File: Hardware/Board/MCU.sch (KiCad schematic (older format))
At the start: 1 part

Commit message: Controller auf 100 Pin Version geändert, Pins ersten Funktionen zugeordnet.
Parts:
- removed U?: STM32L475RGTx, Package_QFP:LQFP-64_10x10mm_P0.5mm, symbol MCU_ST_STM32L4:STM32L475RGTx
- added C? (x2): 100nF, symbol Device:C
- added C? (x4): C, symbol Device:C
- added C?: 10nF, symbol Device:C
- added C?: 1uF, symbol Device:C
- added C?: 10uF, symbol Device:C
- added C? (x2): 5p1, symbol Device:C
- added C? (x2): 8p2, symbol Device:C
- added U?: AT25SF081-XMHD-X, Package_SO:TSSOP-8_4.4x3mm_P0.65mm, symbol Memory_Flash:AT25SF081-XMHD-X
- added U?: STM32L475VGTx, Package_QFP:LQFP-100_14x14mm_P0.5mm, symbol MCU_ST_STM32L4:STM32L475VGTx
- added Y?: 32.768, symbol Device:Crystal
- added Y?: 8MHz, symbol Device:Crystal
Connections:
- net labels added: +3.3V, GND, JTAG_RES, JTAG_TCK, JTAG_TDI, JTAG_TDO, JTAG_TMS, QuadSPI_CLK, QuadSPI_IO0, QuadSPI_IO1, QuadSPI_IO2, QuadSPI_IO3, QuadSPI_NCS, RxD-LIN1, RxD-LIN2, RxD-LIN3, RxD-RS485, SCL-1WIRE, SDA-1WIRE, TxD-LIN1, TxD-LIN2, TxD-LIN3, TxD-RS485, USB_D+, USB_D-, USB_ID, USB_NOE, USB_SOF
- wire segments 2 -> 94

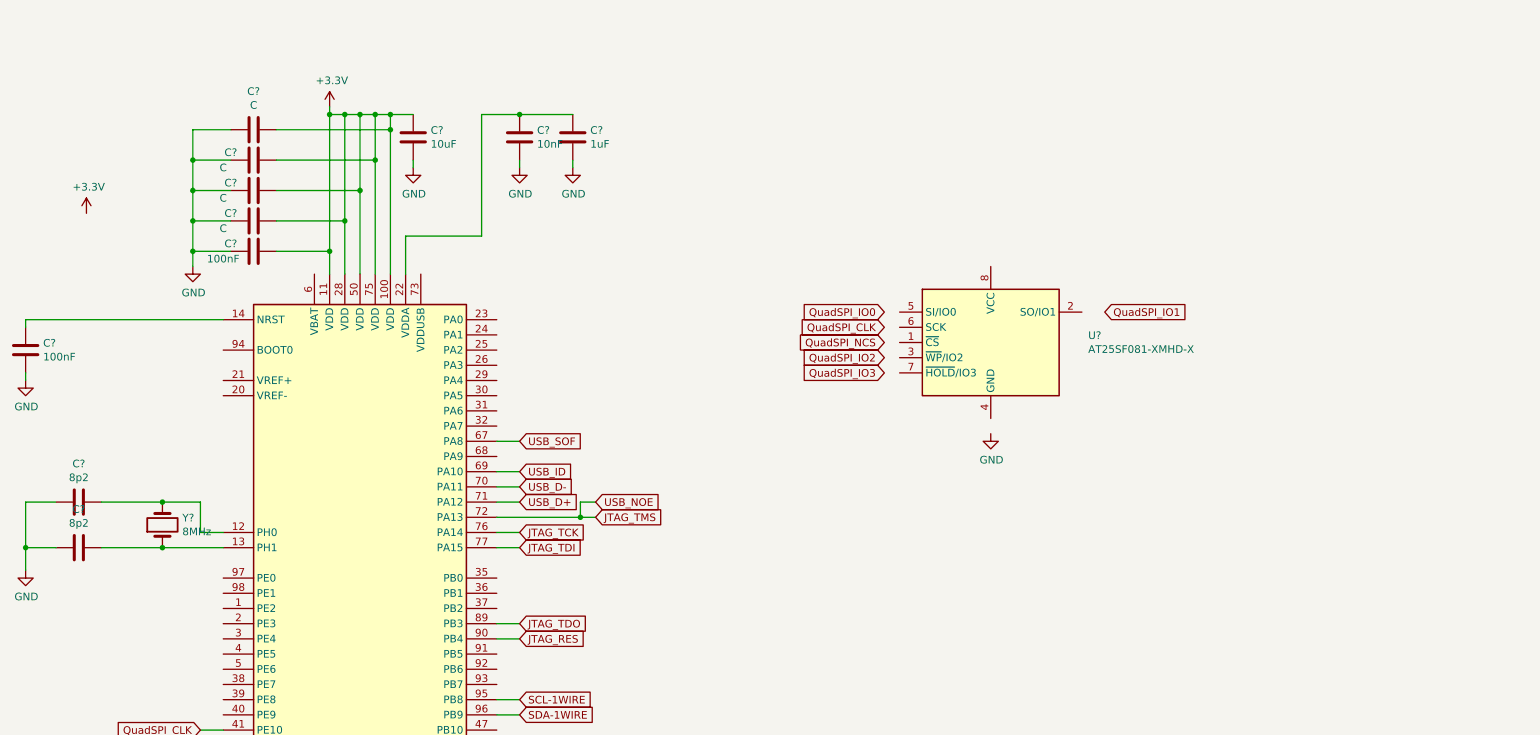
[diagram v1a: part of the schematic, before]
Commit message: JTAG und USB Anschlüsse zugefügt
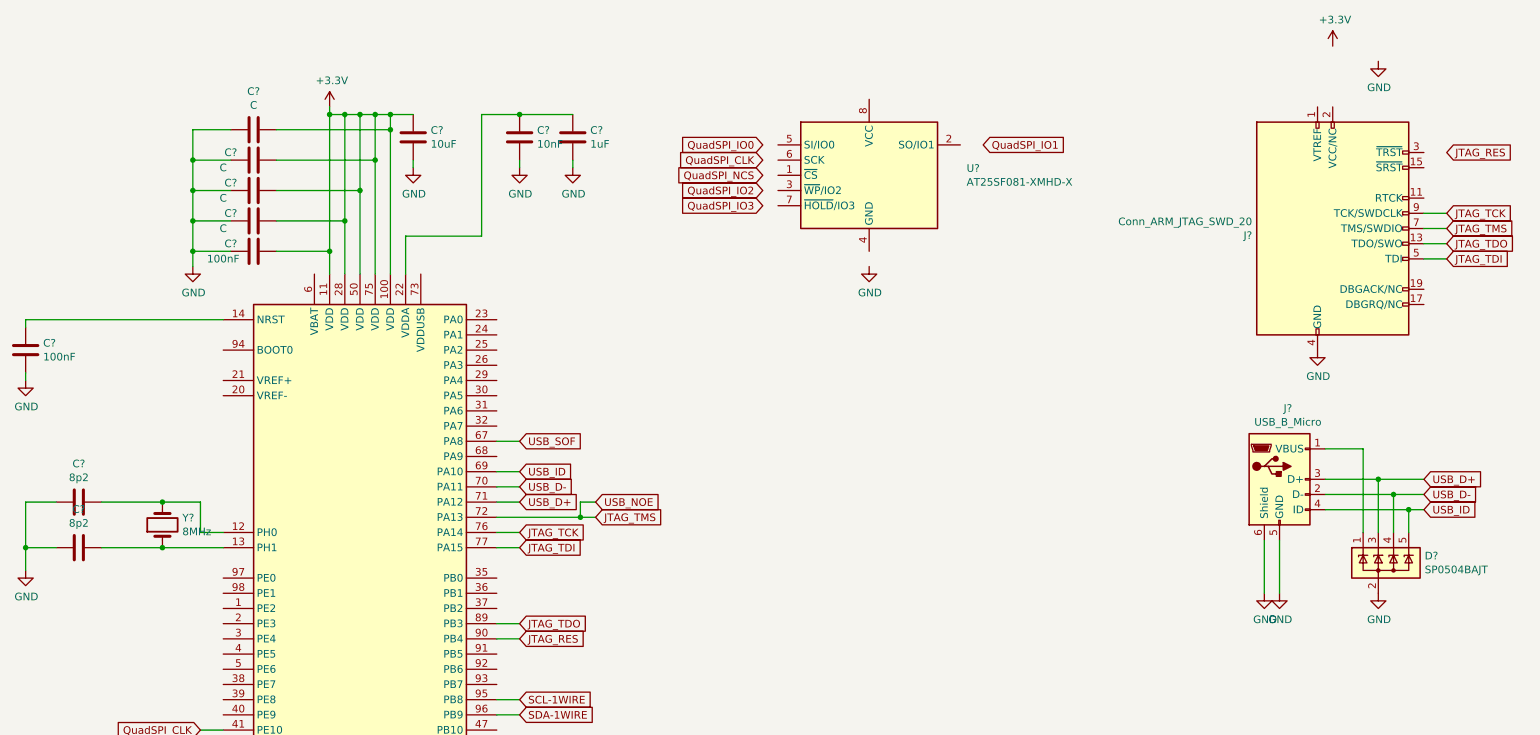
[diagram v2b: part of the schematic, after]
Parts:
- added D?: SP0504BAJT, Package_TO_SOT_SMD:SOT-353_SC-70-5, symbol Power_Protection:SP0504BAJT
- added J?: USB_B_Micro, symbol Connector:USB_B_Micro
- added J?: Conn_ARM_JTAG_SWD_20, symbol Connector:Conn_ARM_JTAG_SWD_20
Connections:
- net GND: now also D?.2 (A), J?.10 (GND), J?.12 (GND), J?.14 (GND), J?.16 (GND), J?.18 (GND), J?.20 (GND), J?.4 (GND), J?.5 (GND), J?.6 (GND), J?.6 (Shield), J?.8 (GND)
- net JTAG_TCK: now also J?.9 (TCK/SWDCLK)
- net JTAG_TDI: now also J?.5 (TDI)
- net JTAG_TDO: now also J?.13 (TDO/SWO)
- net JTAG_TMS: now also J?.7 (TMS/SWDIO)
- net USB_D+: now also D?.3 (K), J?.3 (D+)
- net USB_D-: now also D?.4 (K), J?.2 (D-)
- net USB_ID: now also D?.5 (K), J?.4 (ID)
- new net: D?.1 (K), J?.1 (VBUS)
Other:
- moved on the sheet: U?
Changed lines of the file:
@@
 L Memory_Flash:AT25SF081-XMHD-X U?
 U 1 1 5C9E12E3
-P 7600 2350
-F 0 "U?" H 8241 2396 50  0000 L CNN
-F 1 "AT25SF081-XMHD-X" H 8241 2305 50  0000 L CNN
-F 2 "Package_SO:TSSOP-8_4.4x3mm_P0.65mm" H 7600 1750 50  0001 C CNN
-F 3 "https://www.adestotech.com/wp-content/uploads/DS-AT25SF081_045.pdf" H 7600 2350 50  0001 C CNN
-	1    7600 2350
+P 6800 1250
+F 0 "U?" H 7441 1296 50  0000 L CNN
+F 1 "AT25SF081-XMHD-X" H 7441 1205 50  0000 L CNN
+F 2 "Package_SO:TSSOP-8_4.4x3mm_P0.65mm" H 6800 650 50  0001 C CNN
+F 3 "https://www.adestotech.com/wp-content/uploads/DS-AT25SF081_045.pdf" H 6800 1250 50  0001 C CNN
+	1    6800 1250
 	1    0    0    -1
 $EndComp
@@
 Text GLabel 2400 5100 0    50   Input ~ 0
 QuadSPI_IO0
-Text GLabel 6900 2550 0    50   Input ~ 0
+Text GLabel 6100 1450 0    50   Input ~ 0
 QuadSPI_IO3
-Text GLabel 6900 2450 0    50   Input ~ 0
+Text GLabel 6100 1350 0    50   Input ~ 0
 QuadSPI_IO2
-Text GLabel 6900 2250 0    50   Input ~ 0
+Text GLabel 6100 1150 0    50   Input ~ 0
 QuadSPI_CLK
-Text GLabel 6900 2350 0    50   Input ~ 0
+Text GLabel 6100 1250 0    50   Input ~ 0
 QuadSPI_NCS
-Text GLabel 8350 2150 2    50   Input ~ 0
+Text GLabel 7550 1050 2    50   Input ~ 0
 QuadSPI_IO1
-Text GLabel 6900 2150 0    50   Input ~ 0
+Text GLabel 6100 1050 0    50   Input ~ 0
 QuadSPI_IO0
 $Comp
 L power:GND #PWR?
 U 1 1 5C9ECC3B
-P 7600 2950
-F 0 "#PWR?" H 7600 2700 50  0001 C CNN
-F 1 "GND" H 7605 2777 50  0000 C CNN
-F 2 "" H 7600 2950 50  0001 C CNN
-F 3 "" H 7600 2950 50  0001 C CNN
-	1    7600 2950
+P 6800 1850
+F 0 "#PWR?" H 6800 1600 50  0001 C CNN
+F 1 "GND" H 6805 1677 50  0000 C CNN
+F 2 "" H 6800 1850 50  0001 C CNN
+F 3 "" H 6800 1850 50  0001 C CNN
+	1    6800 1850
 	1    0    0    -1
 $EndComp
@@
 L power:+3.3V #PWR?
 U 1 1 5CA05987
-P 1650 1500
-F 0 "#PWR?" H 1650 1350 50  0001 C CNN
-F 1 "+3.3V" H 1665 1673 50  0000 C CNN
-F 2 "" H 1650 1500 50  0001 C CNN
-F 3 "" H 1650 1500 50  0001 C CNN
-	1    1650 1500
+P 9850 400
+F 0 "#PWR?" H 9850 250 50  0001 C CNN
+F 1 "+3.3V" H 9865 573 50  0000 C CNN
+F 2 "" H 9850 400 50  0001 C CNN
+F 3 "" H 9850 400 50  0001 C CNN
+	1    9850 400
 	1    0    0    -1
 $EndComp
@@
 Wire Wire Line
 	5800 7300 5800 7450
+$Comp
+L Connector:USB_B_Micro J?
+U 1 1 5CA22A0B
+P 9500 3250
+F 0 "J?" H 9555 3717 50  0000 C CNN
+F 1 "USB_B_Micro" H 9555 3626 50  0000 C CNN
+F 2 "" H 9650 3200 50  0001 C CNN
+F 3 "~" H 9650 3200 50  0001 C CNN
+	1    9500 3250
+	1    0    0    -1
+$EndComp
+$Comp
+L Connector:Conn_ARM_JTAG_SWD_20 J?
+U 1 1 5CA25131
+P 9850 1600
+F 0 "J?" H 9320 1554 50  0000 R CNN
+F 1 "Conn_ARM_JTAG_SWD_20" H 9320 1645 50  0000 R CNN
+F 2 "" H 10300 550 50  0001 L TNN
+F 3 "http://infocenter.arm.com/help/topic/com.arm.doc.dui0499b/DUI0499B_system_design_reference.pdf" V 9500 350 50  0001 C CNN
+	1    9850 1600
+	1    0    0    -1
+$EndComp
+$Comp
+L Power_Protection:SP0504BAJT D?
+U 1 1 5CA2F4B9
+P 10150 3800
+F 0 "D?" H 10455 3846 50  0000 L CNN
+F 1 "SP0504BAJT" H 10455 3755 50  0000 L CNN
+F 2 "Package_TO_SOT_SMD:SOT-353_SC-70-5" H 10450 3750 50  0001 L CNN
+F 3 "http://www.littelfuse.com/~/media/files/littelfuse/technical%20resources/documents/data%20sheets/sp05xxba.pdf" H 10275 3925 50  0001 C CNN
+	1    10150 3800
+	1    0    0    -1
+$EndComp
+Text GLabel 10450 3350 2    50   Input ~ 0
+USB_D-
+Text GLabel 10450 3250 2    50   Input ~ 0
+USB_D+
+Text GLabel 10450 3450 2    50   Input ~ 0
+USB_ID
+$Comp
+L power:GND #PWR?
+U 1 1 5CA3E241
+P 10150 4000
+F 0 "#PWR?" H 10150 3750 50  0001 C CNN
+F 1 "GND" H 10155 3827 50  0000 C CNN
+F 2 "" H 10150 4000 50  0001 C CNN
+F 3 "" H 10150 4000 50  0001 C CNN
+	1    10150 4000
+	1    0    0    -1
+$EndComp
+$Comp
+L power:GND #PWR?
+U 1 1 5CA40A3E
+P 9500 4000
+F 0 "#PWR?" H 9500 3750 50  0001 C CNN
+F 1 "GND" H 9505 3827 50  0000 C CNN
+F 2 "" H 9500 4000 50  0001 C CNN
+F 3 "" H 9500 4000 50  0001 C CNN
+	1    9500 4000
+	1    0    0    -1
+$EndComp
+$Comp
+L power:GND #PWR?
+U 1 1 5CA431EB
+P 9400 4000
+F 0 "#PWR?" H 9400 3750 50  0001 C CNN
+F 1 "GND" H 9405 3827 50  0000 C CNN
+F 2 "" H 9400 4000 50  0001 C CNN
+F 3 "" H 9400 4000 50  0001 C CNN
+	1    9400 4000
+	1    0    0    -1
+$EndComp
+Wire Wire Line
+	9500 3650 9500 4000
+Wire Wire Line
+	9400 3650 9400 4000
+Wire Wire Line
+	9800 3250 10150 3250
+Wire Wire Line
+	9800 3350 10250 3350
+Wire Wire Line
+	9800 3450 10350 3450
+Wire Wire Line
+	10050 3600 10050 3050
+Wire Wire Line
+	10050 3050 9800 3050
+Wire Wire Line
+	10150 3600 10150 3250
+Connection ~ 10150 3250
+Wire Wire Line
+	10150 3250 10450 3250
+Wire Wire Line
+	10250 3600 10250 3350
+Connection ~ 10250 3350
+Wire Wire Line
+	10250 3350 10450 3350
+Wire Wire Line
+	10350 3600 10350 3450
+Connection ~ 10350 3450
+Wire Wire Line
+	10350 3450 10450 3450
+Text GLabel 10600 1500 2    50   Input ~ 0
+JTAG_TCK
+Text GLabel 10600 1800 2    50   Input ~ 0
+JTAG_TDI
+Text GLabel 10600 1700 2    50   Input ~ 0
+JTAG_TDO
+Text GLabel 10600 1100 2    50   Input ~ 0
+JTAG_RES
+Text GLabel 10600 1600 2    50   Input ~ 0
+JTAG_TMS
+Wire Wire Line
+	10450 1500 10600 1500
+Wire Wire Line
+	10450 1600 10600 1600
+Wire Wire Line
+	10450 1700 10600 1700
+Wire Wire Line
+	10450 1800 10600 1800
+$Comp
+L power:GND #PWR?
+U 1 1 5CA7FBF5
+P 9750 2400
+F 0 "#PWR?" H 9750 2150 50  0001 C CNN
+F 1 "GND" H 9755 2227 50  0000 C CNN
+F 2 "" H 9750 2400 50  0001 C CNN
+F 3 "" H 9750 2400 50  0001 C CNN
+	1    9750 2400
+	1    0    0    -1
+$EndComp
+$Comp
+L power:GND #PWR?
+U 1 1 5CA82F31
+P 10150 500
+F 0 "#PWR?" H 10150 250 50  0001 C CNN
+F 1 "GND" H 10155 327 50  0000 C CNN
+F 2 "" H 10150 500 50  0001 C CNN
+F 3 "" H 10150 500 50  0001 C CNN
+	1    10150 500
+	1    0    0    -1
+$EndComp
 $EndSCHEMATC

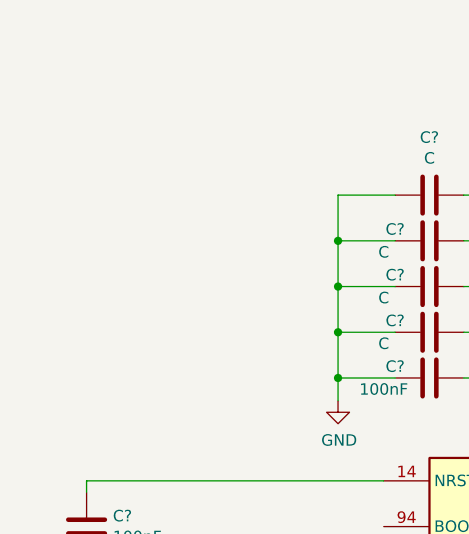
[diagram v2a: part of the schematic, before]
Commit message: Schaltregler Design fertig gestellt, Datenblätter hinzu gefügt.
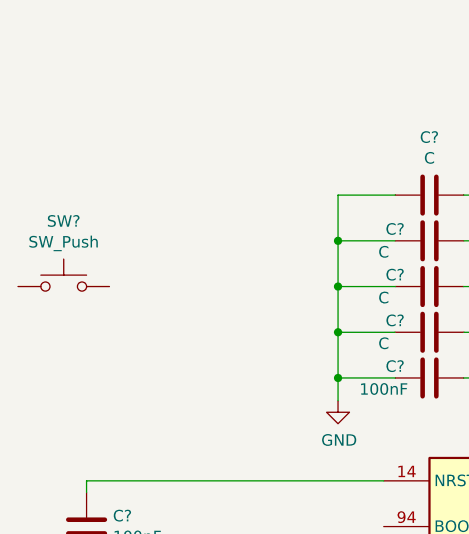
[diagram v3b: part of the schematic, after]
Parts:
- added SW?: SW_Push, symbol Switch:SW_Push
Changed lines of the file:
@@
+	1    0    0    -1
+$EndComp
+$Comp
+L Switch:SW_Push SW?
+U 1 1 5CA4B2AF
+P 1150 1350
+F 0 "SW?" H 1150 1635 50  0000 C CNN
+F 1 "SW_Push" H 1150 1544 50  0000 C CNN
+F 2 "" H 1150 1550 50  0001 C CNN
+F 3 "" H 1150 1550 50  0001 C CNN
+	1    1150 1350
 	1    0    0    -1
 $EndComp

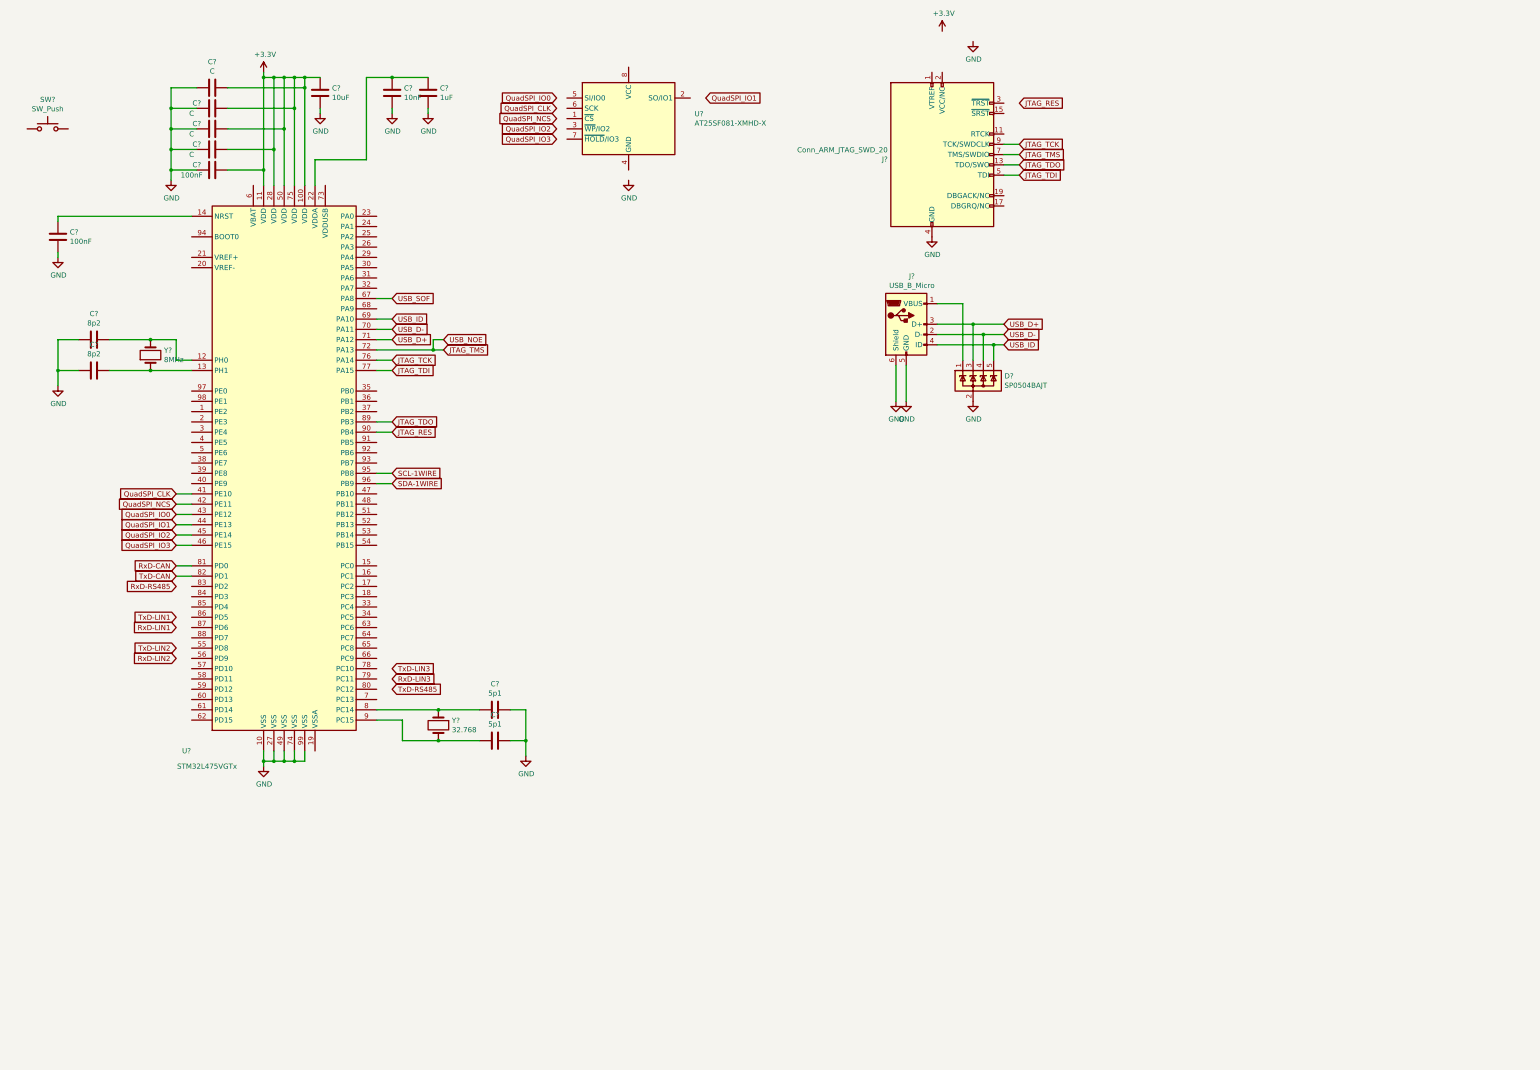
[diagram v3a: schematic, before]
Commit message: FTDI EVE Touch hinzugefügt
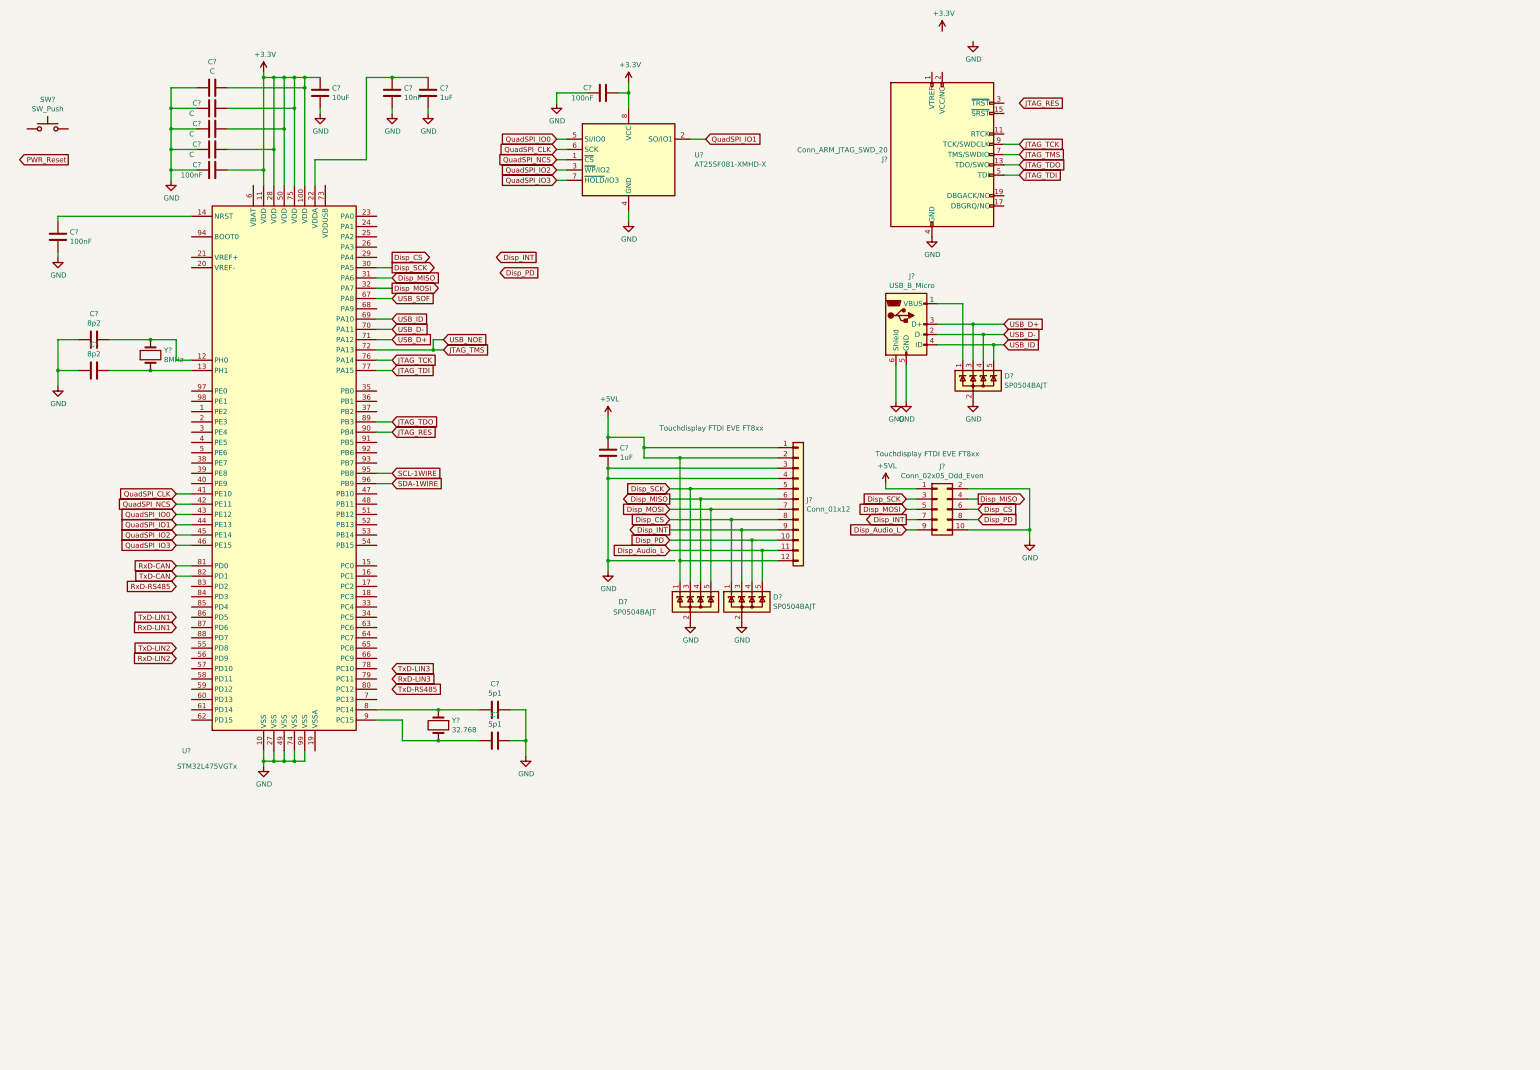
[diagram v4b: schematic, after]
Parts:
- added C?: 1uF, symbol Device:C
- added C?: 100nF, symbol Device:C
- added D? (x2): SP0504BAJT, Package_TO_SOT_SMD:SOT-353_SC-70-5, symbol Power_Protection:SP0504BAJT
- added J?: Conn_02x05_Odd_Even, symbol Connector_Generic:Conn_02x05_Odd_Even
- added J?: Conn_01x12, symbol Connector_Generic:Conn_01x12
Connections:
- net +3V3: now also U?.8 (VCC), C?.1
- net GND: now also U?.4 (GND), C?.2, C?.2, D?.2 (A), D?.2 (A), J?.10 (Pin_10), J?.2 (Pin_2), J?.3 (Pin_3), J?.4 (Pin_4)
- net QuadSPI_CLK: now also U?.6 (SCK)
- net QuadSPI_IO0: now also U?.5 (SI/IO0)
- net QuadSPI_IO1: now also U?.2 (SO/IO1)
- net QuadSPI_IO2: now also U?.3 (~WP~/IO2)
- net QuadSPI_IO3: now also U?.7 (~HOLD~/IO3)
- net QuadSPI_NCS: now also U?.1 (~CS)
- net Disp_SCK: now reaches U?.30 (PA5)
- net Disp_SCK: now also D?.3 (K), J?.3 (Pin_3), J?.5 (Pin_5)
- net Disp_MISO: now reaches U?.31 (PA6)
- net Disp_MISO: now also D?.4 (K), J?.4 (Pin_4), J?.6 (Pin_6)
- net Disp_MOSI: now reaches U?.32 (PA7)
- net Disp_MOSI: now also D?.5 (K), J?.5 (Pin_5), J?.7 (Pin_7)
- new net +5VL: C?.1, D?.1 (K), J?.1 (Pin_1), J?.1 (Pin_1), J?.12 (Pin_12), J?.2 (Pin_2)
- new net Disp_Audio_L: D?.5 (K), J?.11 (Pin_11), J?.9 (Pin_9)
- new net Disp_CS: D?.1 (K), J?.6 (Pin_6), J?.8 (Pin_8)
- new net Disp_INT: D?.3 (K), J?.7 (Pin_7), J?.9 (Pin_9)
- new net Disp_PD: D?.4 (K), J?.10 (Pin_10), J?.8 (Pin_8)
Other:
- note added: "Touchdisplay FTDI EVE FT8xx"
- moved on the sheet: U?
